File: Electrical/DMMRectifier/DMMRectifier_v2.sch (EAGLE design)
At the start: 19 parts, among them IC1 TL074D

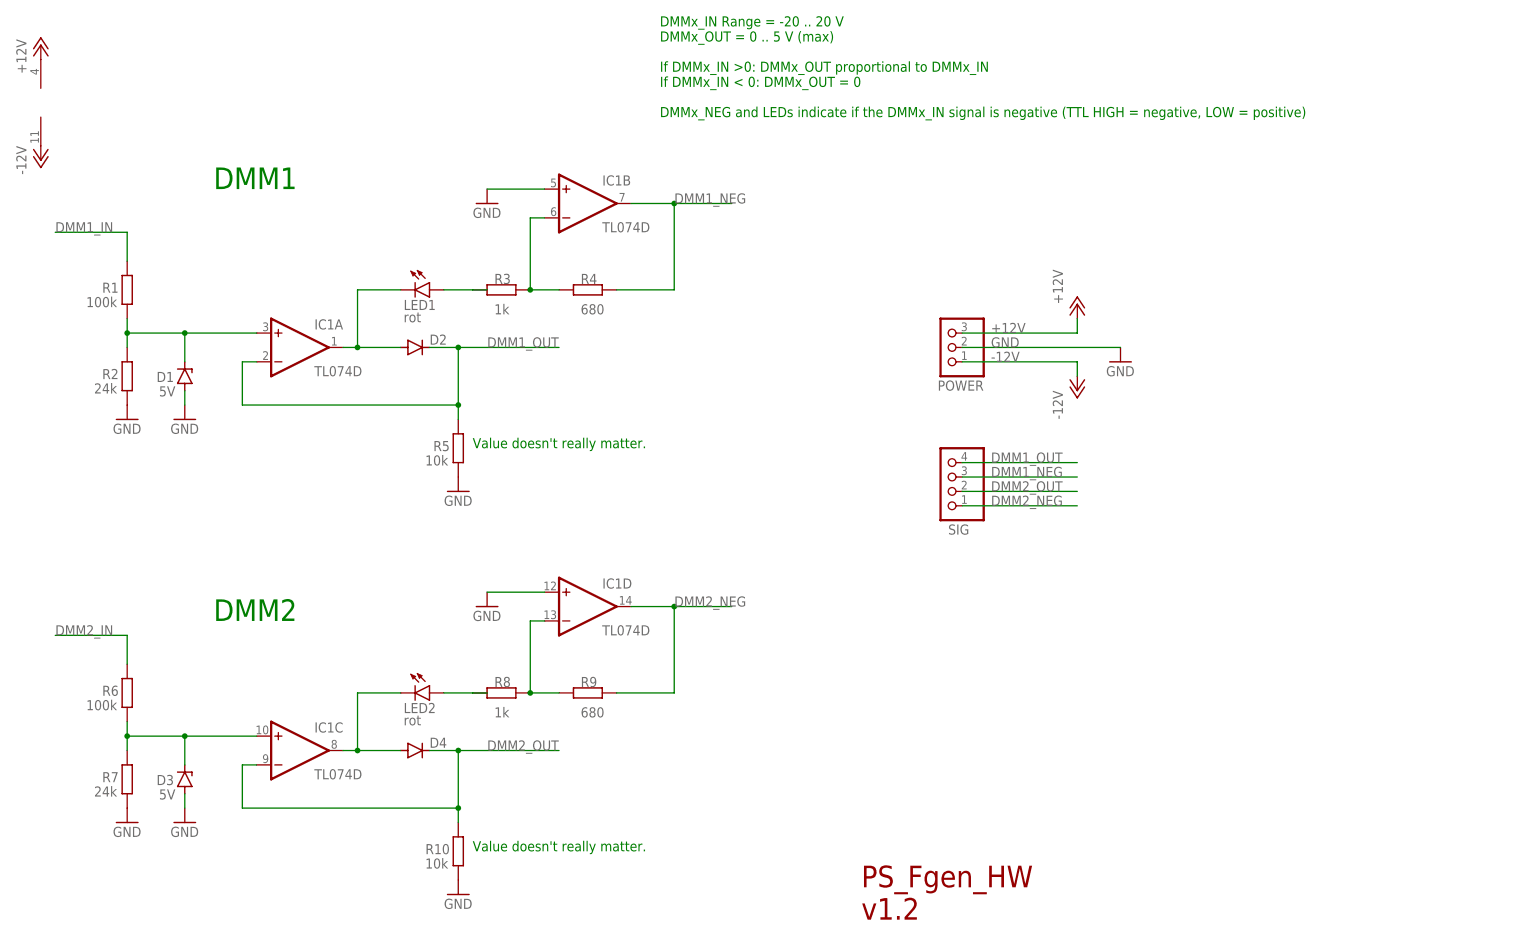
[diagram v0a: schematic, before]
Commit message: Updated FrontPanel and DMMRectifier in Electrical folder
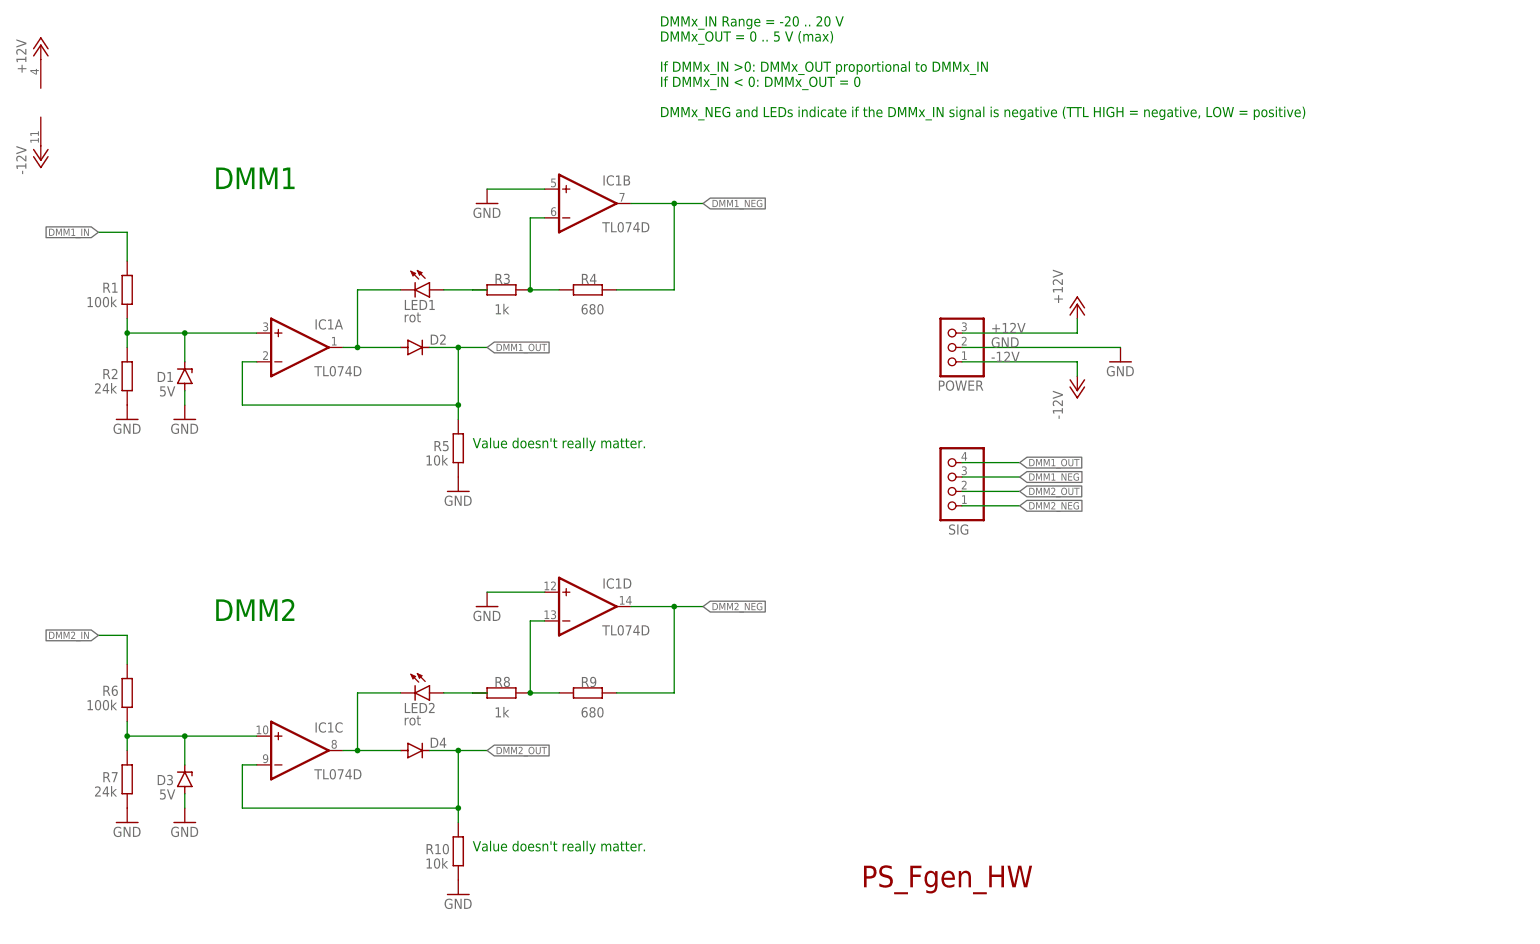
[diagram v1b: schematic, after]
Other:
- note added: "PS_Fgen_HW"
- note removed: "PS_Fgen_HW v1.2"
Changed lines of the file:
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@@
 <?xml version="1.0" encoding="utf-8"?>
 <!DOCTYPE eagle SYSTEM "eagle.dtd">
-<eagle version="9.6.2">
+<eagle version="9.7.0">
 <drawing>
 <settings>
@@
 <layer number="18" name="Vias" color="2" fill="1" visible="no" active="no"/>
 <layer number="19" name="Unrouted" color="6" fill="1" visible="no" active="no"/>
-<layer number="20" name="Dimension" color="15" fill="1" visible="no" active="no"/>
+<layer number="20" name="Dimension" color="24" fill="1" visible="no" active="no"/>
 <layer number="21" name="tPlace" color="7" fill="1" visible="no" active="no"/>
 <layer number="22" name="bPlace" color="7" fill="1" visible="no" active="no"/>
@@
 <layer number="97" name="Info" color="7" fill="1" visible="yes" active="yes"/>
 <layer number="98" name="Guide" color="6" fill="1" visible="yes" active="yes"/>
-<layer number="99" name="SpiceOrder" color="5" fill="1" visible="yes" active="yes"/>
+<layer number="99" name="SpiceOrder" color="7" fill="1" visible="yes" active="yes"/>
 </layers>
 <schematic xreflabel="%F%N/%S.%C%R" xrefpart="/%S.%C%R">
@@
 <sheet>
 <plain>
-<text x="165.1" y="20.32" size="3.81" layer="94" align="top-left">PS_Fgen_HW
-v1.2</text>
+<text x="165.1" y="20.32" size="3.81" layer="94" align="top-left">PS_Fgen_HW</text>
 <text x="129.54" y="152.4" size="1.778" layer="91">DMMx_IN Range = -20 .. 20 V
 DMMx_OUT = 0 .. 5 V (max)
@@
 <pinref part="D2" gate="G$1" pin="C"/>
 <wire x1="88.9" y1="111.76" x2="93.98" y2="111.76" width="0.1524" layer="91"/>
-<label x="99.06" y="111.76" size="1.778" layer="95"/>
 <pinref part="IC1" gate="A" pin="-IN"/>
-<wire x1="93.98" y1="111.76" x2="111.76" y2="111.76" width="0.1524" layer="91"/>
+<wire x1="93.98" y1="111.76" x2="99.06" y2="111.76" width="0.1524" layer="91"/>
 <wire x1="58.42" y1="109.22" x2="55.88" y2="109.22" width="0.1524" layer="91"/>
 <wire x1="55.88" y1="109.22" x2="55.88" y2="101.6" width="0.1524" layer="91"/>
 <wire x1="55.88" y1="101.6" x2="93.98" y2="101.6" width="0.1524" layer="91"/>
 <wire x1="93.98" y1="101.6" x2="93.98" y2="111.76" width="0.1524" layer="91"/>
-<junction x="93.98" y="111.76"/>
 <pinref part="R5" gate="G$1" pin="2"/>
 <wire x1="93.98" y1="99.06" x2="93.98" y2="101.6" width="0.1524" layer="91"/>
+<label x="99.06" y="111.76" size="1.27" layer="95" xref="yes"/>
+<junction x="93.98" y="111.76"/>
 <junction x="93.98" y="101.6"/>
 </segment>
 <segment>
 <pinref part="SIG" gate="A" pin="4"/>
-<wire x1="182.88" y1="91.44" x2="203.2" y2="91.44" width="0.1524" layer="91"/>
-<label x="187.96" y="91.44" size="1.778" layer="95"/>
+<wire x1="182.88" y1="91.44" x2="193.04" y2="91.44" width="0.1524" layer="91"/>
+<label x="193.04" y="91.44" size="1.27" layer="95" xref="yes"/>
 </segment>
 </net>
@@
 <pinref part="R1" gate="G$1" pin="2"/>
 <wire x1="35.56" y1="127" x2="35.56" y2="132.08" width="0.1524" layer="91"/>
-<wire x1="35.56" y1="132.08" x2="22.86" y2="132.08" width="0.1524" layer="91"/>
-<label x="22.86" y="132.08" size="1.778" layer="95"/>
+<wire x1="35.56" y1="132.08" x2="30.48" y2="132.08" width="0.1524" layer="91"/>
+<label x="30.48" y="132.08" size="1.27" layer="95" rot="R180" xref="yes"/>
 </segment>
 </net>
@@
 <wire x1="132.08" y1="137.16" x2="132.08" y2="121.92" width="0.1524" layer="91"/>
 <wire x1="132.08" y1="121.92" x2="121.92" y2="121.92" width="0.1524" layer="91"/>
-<wire x1="132.08" y1="137.16" x2="142.24" y2="137.16" width="0.1524" layer="91"/>
+<wire x1="132.08" y1="137.16" x2="137.16" y2="137.16" width="0.1524" layer="91"/>
+<label x="137.16" y="137.16" size="1.27" layer="95" xref="yes"/>
 <junction x="132.08" y="137.16"/>
-<label x="132.08" y="137.16" size="1.778" layer="95"/>
 </segment>
 <segment>
 <pinref part="SIG" gate="A" pin="3"/>
-<wire x1="182.88" y1="88.9" x2="203.2" y2="88.9" width="0.1524" layer="91"/>
-<label x="187.96" y="88.9" size="1.778" layer="95"/>
+<wire x1="182.88" y1="88.9" x2="193.04" y2="88.9" width="0.1524" layer="91"/>
+<label x="193.04" y="88.9" size="1.27" layer="95" xref="yes"/>
 </segment>
 </net>
@@
 <pinref part="R6" gate="G$1" pin="2"/>
 <wire x1="35.56" y1="55.88" x2="35.56" y2="60.96" width="0.1524" layer="91"/>
-<wire x1="35.56" y1="60.96" x2="22.86" y2="60.96" width="0.1524" layer="91"/>
-<label x="22.86" y="60.96" size="1.778" layer="95"/>
+<wire x1="35.56" y1="60.96" x2="30.48" y2="60.96" width="0.1524" layer="91"/>
+<label x="30.48" y="60.96" size="1.27" layer="95" rot="R180" xref="yes"/>
 </segment>
 </net>
@@
 <pinref part="D4" gate="G$1" pin="C"/>
 <wire x1="88.9" y1="40.64" x2="93.98" y2="40.64" width="0.1524" layer="91"/>
-<label x="99.06" y="40.64" size="1.778" layer="95"/>
 <pinref part="IC1" gate="C" pin="-IN"/>
-<wire x1="93.98" y1="40.64" x2="111.76" y2="40.64" width="0.1524" layer="91"/>
+<wire x1="93.98" y1="40.64" x2="99.06" y2="40.64" width="0.1524" layer="91"/>
 <wire x1="58.42" y1="38.1" x2="55.88" y2="38.1" width="0.1524" layer="91"/>
 <wire x1="55.88" y1="38.1" x2="55.88" y2="30.48" width="0.1524" layer="91"/>
 <wire x1="55.88" y1="30.48" x2="93.98" y2="30.48" width="0.1524" layer="91"/>
 <wire x1="93.98" y1="30.48" x2="93.98" y2="40.64" width="0.1524" layer="91"/>
-<junction x="93.98" y="40.64"/>
 <pinref part="R10" gate="G$1" pin="2"/>
 <wire x1="93.98" y1="27.94" x2="93.98" y2="30.48" width="0.1524" layer="91"/>
+<label x="99.06" y="40.64" size="1.27" layer="95" xref="yes"/>
+<junction x="93.98" y="40.64"/>
 <junction x="93.98" y="30.48"/>
 </segment>
 <segment>
 <pinref part="SIG" gate="A" pin="2"/>
-<wire x1="182.88" y1="86.36" x2="203.2" y2="86.36" width="0.1524" layer="91"/>
-<label x="187.96" y="86.36" size="1.778" layer="95"/>
+<wire x1="182.88" y1="86.36" x2="193.04" y2="86.36" width="0.1524" layer="91"/>
+<label x="193.04" y="86.36" size="1.27" layer="95" xref="yes"/>
 </segment>
 </net>
@@
 <wire x1="132.08" y1="66.04" x2="132.08" y2="50.8" width="0.1524" layer="91"/>
 <wire x1="132.08" y1="50.8" x2="121.92" y2="50.8" width="0.1524" layer="91"/>
-<wire x1="132.08" y1="66.04" x2="142.24" y2="66.04" width="0.1524" layer="91"/>
+<wire x1="132.08" y1="66.04" x2="137.16" y2="66.04" width="0.1524" layer="91"/>
+<pinref part="IC1" gate="D" pin="OUT"/>
+<label x="137.16" y="66.04" size="1.27" layer="95" xref="yes"/>
 <junction x="132.08" y="66.04"/>
-<label x="132.08" y="66.04" size="1.778" layer="95"/>
-<pinref part="IC1" gate="D" pin="OUT"/>
 </segment>
 <segment>
 <pinref part="SIG" gate="A" pin="1"/>
-<wire x1="182.88" y1="83.82" x2="203.2" y2="83.82" width="0.1524" layer="91"/>
-<label x="187.96" y="83.82" size="1.778" layer="95"/>
-</segment>
-</net>
+<wire x1="182.88" y1="83.82" x2="193.04" y2="83.82" width="0.1524" layer="91"/>
+<label x="193.04" y="83.82" size="1.27" layer="95" xref="yes"/>
+</segment>
+</net>
